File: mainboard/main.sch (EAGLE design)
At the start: 4 parts, among them J1 501645-2620, J2 RJHSE-3380, J3 RJHSE-3380

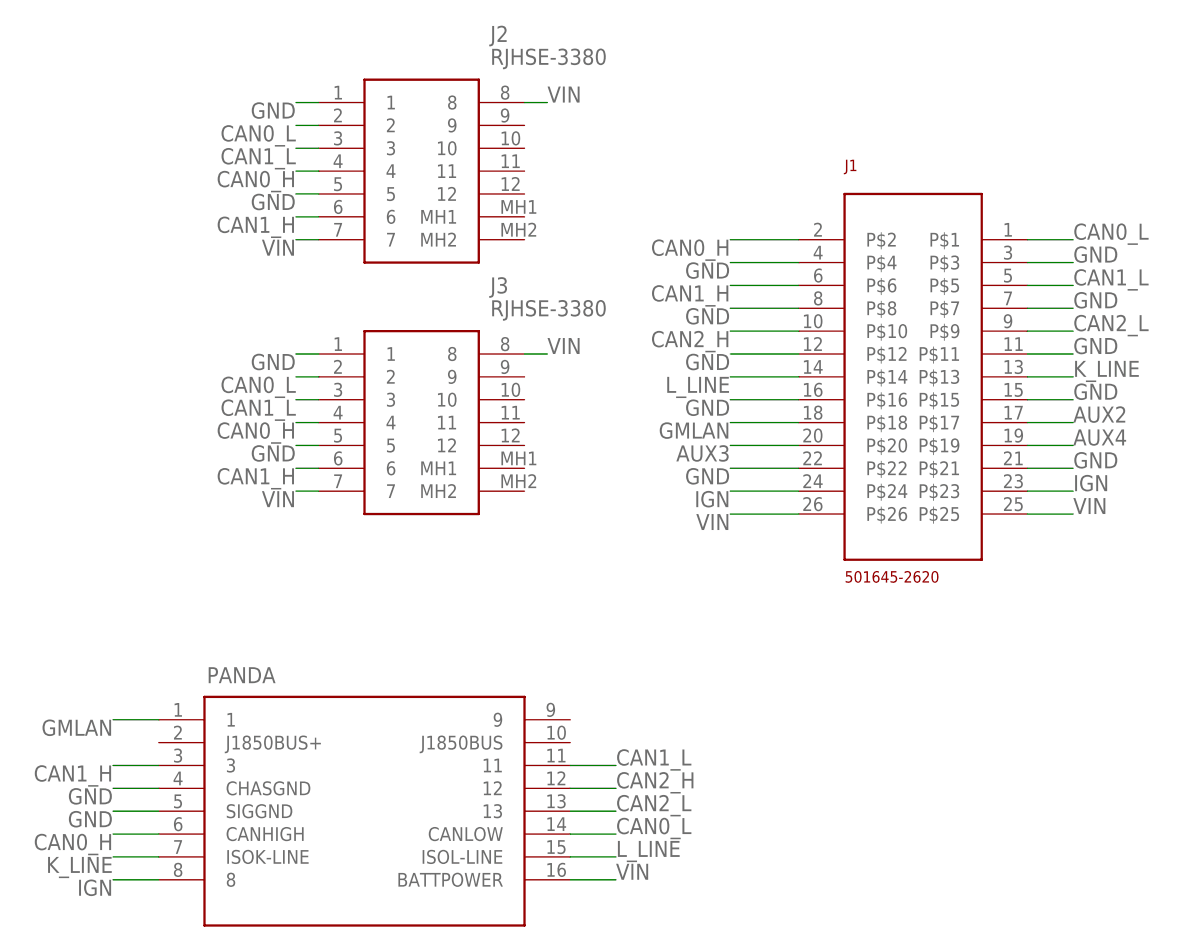
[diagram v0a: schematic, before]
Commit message: switch to rj45 for the interconnect
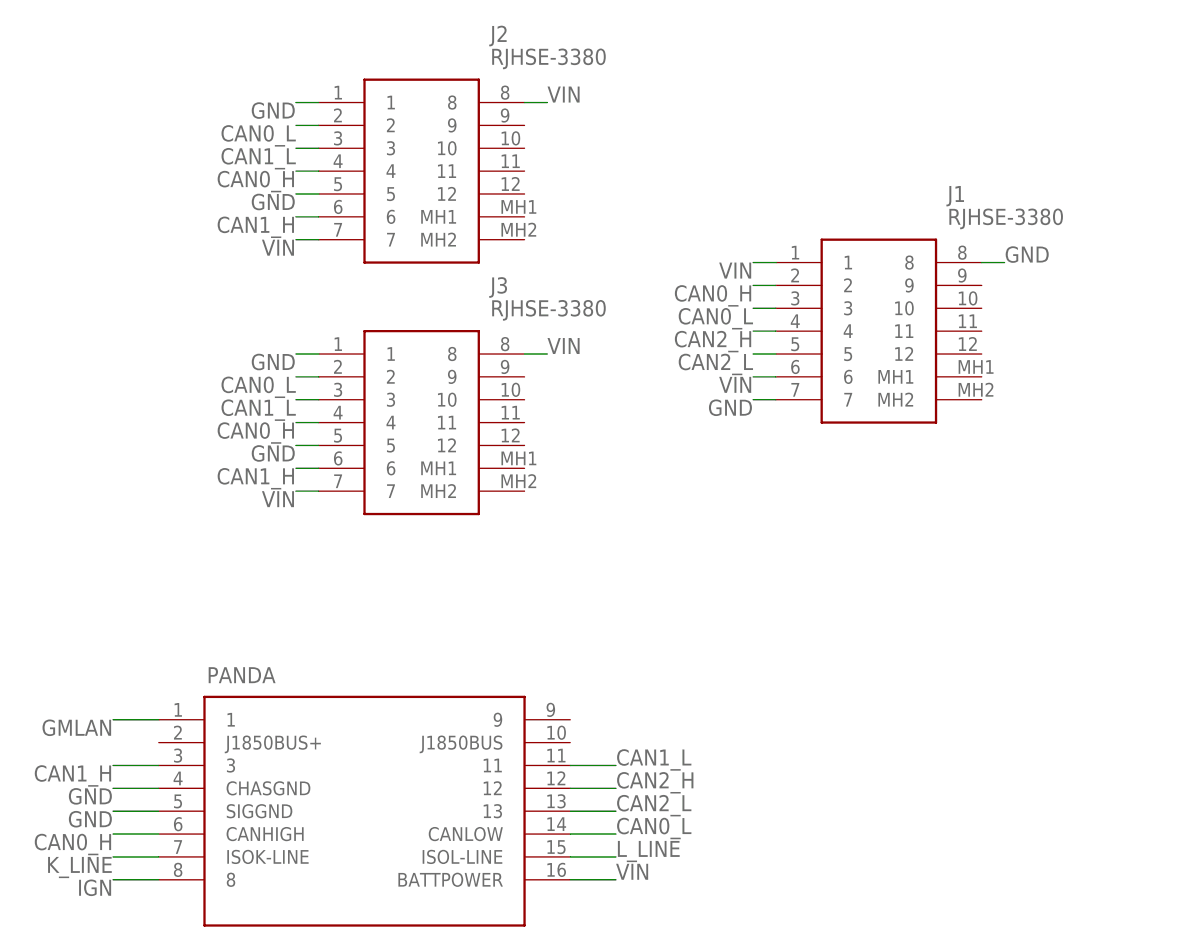
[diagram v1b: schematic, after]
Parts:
- J1: value 501645-2620 -> RJHSE-3380; device Souers:501645-2620 -> RJHSE-3380:RJHSE-3380
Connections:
- removed net AUX2: J1.P$17
- removed net AUX3: J1.P$20
- removed net AUX4: J1.P$19
- net CAN0_H: now also J1.2; no longer J1.P$2
- net CAN0_L: now also J1.3; no longer J1.P$1
- net CAN1_H: no longer J1.P$6
- net CAN1_L: no longer J1.P$5
- net CAN2_H: now also J1.4; no longer J1.P$10
- net CAN2_L: now also J1.5; no longer J1.P$9
- net GMLAN: no longer J1.P$18
- net GND: now also J1.7, J1.8; no longer J1.P$11, J1.P$12, J1.P$15, J1.P$16, J1.P$21, J1.P$22, J1.P$3, J1.P$4, J1.P$7, J1.P$8
- net IGN: no longer J1.P$23, J1.P$24
- net K_LINE: no longer J1.P$13
- net L_LINE: no longer J1.P$14
- net VIN: now also J1.1, J1.6; no longer J1.P$25, J1.P$26
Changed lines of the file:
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@@
 <parts>
 <part name="PANDA" library="comma.ai" deviceset="OBDII-FEMALE" device="FEMALE"/>
-<part name="J1" library="Souers" deviceset="501645-2620" device=""/>
 <part name="J2" library="RJHSE-3380" deviceset="RJHSE-3380" device=""/>
 <part name="J3" library="RJHSE-3380" deviceset="RJHSE-3380" device=""/>
+<part name="J1" library="RJHSE-3380" deviceset="RJHSE-3380" device=""/>
 </parts>
 <sheets>
@@
 <instances>
 <instance part="PANDA" gate="G$1" x="-25.4" y="12.7"/>
-<instance part="J1" gate="G$1" x="30.48" y="58.42"/>
 <instance part="J2" gate="G$1" x="-30.48" y="91.44"/>
 <instance part="J3" gate="G$1" x="-30.48" y="63.5"/>
+<instance part="J1" gate="G$1" x="20.32" y="73.66"/>
 </instances>
 <busses>
@@
 </segment>
 <segment>
-<pinref part="J1" gate="G$1" pin="P$3"/>
-<wire x1="48.26" y1="73.66" x2="53.34" y2="73.66" width="0.1524" layer="91"/>
-<label x="53.34" y="73.66" size="1.778" layer="95"/>
-</segment>
-<segment>
-<pinref part="J1" gate="G$1" pin="P$4"/>
-<wire x1="22.86" y1="73.66" x2="15.24" y2="73.66" width="0.1524" layer="91"/>
-<label x="15.24" y="73.66" size="1.778" layer="95" rot="R180"/>
-</segment>
-<segment>
-<pinref part="J1" gate="G$1" pin="P$8"/>
-<wire x1="22.86" y1="68.58" x2="15.24" y2="68.58" width="0.1524" layer="91"/>
-<label x="15.24" y="68.58" size="1.778" layer="95" rot="R180"/>
-</segment>
-<segment>
-<pinref part="J1" gate="G$1" pin="P$7"/>
-<wire x1="48.26" y1="68.58" x2="53.34" y2="68.58" width="0.1524" layer="91"/>
-<label x="53.34" y="68.58" size="1.778" layer="95"/>
-</segment>
-<segment>
-<pinref part="J1" gate="G$1" pin="P$11"/>
-<wire x1="48.26" y1="63.5" x2="53.34" y2="63.5" width="0.1524" layer="91"/>
-<label x="53.34" y="63.5" size="1.778" layer="95"/>
-</segment>
-<segment>
-<pinref part="J1" gate="G$1" pin="P$12"/>
-<wire x1="22.86" y1="63.5" x2="15.24" y2="63.5" width="0.1524" layer="91"/>
-<label x="15.24" y="63.5" size="1.778" layer="95" rot="R180"/>
-</segment>
-<segment>
-<pinref part="J1" gate="G$1" pin="P$21"/>
-<wire x1="48.26" y1="50.8" x2="53.34" y2="50.8" width="0.1524" layer="91"/>
-<label x="53.34" y="50.8" size="1.778" layer="95"/>
-</segment>
-<segment>
-<pinref part="J1" gate="G$1" pin="P$22"/>
-<wire x1="22.86" y1="50.8" x2="15.24" y2="50.8" width="0.1524" layer="91"/>
-<label x="15.24" y="50.8" size="1.778" layer="95" rot="R180"/>
-</segment>
-<segment>
-<pinref part="J1" gate="G$1" pin="P$16"/>
-<wire x1="22.86" y1="58.42" x2="15.24" y2="58.42" width="0.1524" layer="91"/>
-<label x="15.24" y="58.42" size="1.778" layer="95" rot="R180"/>
-</segment>
-<segment>
-<pinref part="J1" gate="G$1" pin="P$15"/>
-<wire x1="48.26" y1="58.42" x2="53.34" y2="58.42" width="0.1524" layer="91"/>
-<label x="53.34" y="58.42" size="1.778" layer="95"/>
-</segment>
-<segment>
 <pinref part="J2" gate="G$1" pin="1"/>
 <wire x1="-30.48" y1="91.44" x2="-33.02" y2="91.44" width="0.1524" layer="91"/>
@@
 <label x="-33.02" y="53.34" size="1.778" layer="95" rot="R180"/>
 </segment>
+<segment>
+<pinref part="J1" gate="G$1" pin="8"/>
+<wire x1="43.18" y1="73.66" x2="45.72" y2="73.66" width="0.1524" layer="91"/>
+<label x="45.72" y="73.66" size="1.778" layer="95"/>
+</segment>
+<segment>
+<pinref part="J1" gate="G$1" pin="7"/>
+<wire x1="20.32" y1="58.42" x2="17.78" y2="58.42" width="0.1524" layer="91"/>
+<label x="17.78" y="58.42" size="1.778" layer="95" rot="R180"/>
+</segment>
 </net>
 <net name="L_LINE" class="0">
@@
 <label x="2.54" y="7.62" size="1.778" layer="95"/>
 </segment>
-<segment>
-<pinref part="J1" gate="G$1" pin="P$14"/>
-<wire x1="22.86" y1="60.96" x2="15.24" y2="60.96" width="0.1524" layer="91"/>
-<label x="15.24" y="60.96" size="1.778" layer="95" rot="R180"/>
-</segment>
 </net>
 <net name="K_LINE" class="0">
@@
 <label x="-53.34" y="7.62" size="1.778" layer="95" rot="R180"/>
 </segment>
-<segment>
-<pinref part="J1" gate="G$1" pin="P$13"/>
-<wire x1="48.26" y1="60.96" x2="53.34" y2="60.96" width="0.1524" layer="91"/>
-<label x="53.34" y="60.96" size="1.778" layer="95"/>
-</segment>
 </net>
 <net name="IGN" class="1">
@@
 <label x="-53.34" y="5.08" size="1.778" layer="95" rot="R180"/>
 </segment>
-<segment>
-<pinref part="J1" gate="G$1" pin="P$23"/>
-<wire x1="48.26" y1="48.26" x2="53.34" y2="48.26" width="0.1524" layer="91"/>
-<label x="53.34" y="48.26" size="1.778" layer="95"/>
-</segment>
-<segment>
-<pinref part="J1" gate="G$1" pin="P$24"/>
-<wire x1="22.86" y1="48.26" x2="15.24" y2="48.26" width="0.1524" layer="91"/>
-<label x="15.24" y="48.26" size="1.778" layer="95" rot="R180"/>
-</segment>
 </net>
 <net name="VIN" class="1">
@@
 </segment>
 <segment>
-<pinref part="J1" gate="G$1" pin="P$25"/>
-<wire x1="48.26" y1="45.72" x2="53.34" y2="45.72" width="0.1524" layer="91"/>
-<label x="53.34" y="45.72" size="1.778" layer="95"/>
-</segment>
-<segment>
-<pinref part="J1" gate="G$1" pin="P$26"/>
-<wire x1="22.86" y1="45.72" x2="15.24" y2="45.72" width="0.1524" layer="91"/>
-<label x="15.24" y="45.72" size="1.778" layer="95" rot="R180"/>
-</segment>
-<segment>
 <pinref part="J2" gate="G$1" pin="7"/>
 <wire x1="-30.48" y1="76.2" x2="-33.02" y2="76.2" width="0.1524" layer="91"/>
@@
 <label x="-5.08" y="63.5" size="1.778" layer="95"/>
 </segment>
+<segment>
+<pinref part="J1" gate="G$1" pin="1"/>
+<wire x1="20.32" y1="73.66" x2="17.78" y2="73.66" width="0.1524" layer="91"/>
+<label x="17.78" y="73.66" size="1.778" layer="95" rot="R180"/>
+</segment>
+<segment>
+<pinref part="J1" gate="G$1" pin="6"/>
+<wire x1="20.32" y1="60.96" x2="17.78" y2="60.96" width="0.1524" layer="91"/>
+<label x="17.78" y="60.96" size="1.778" layer="95" rot="R180"/>
+</segment>
 </net>
 <net name="CAN2_H" class="0">
@@
 </segment>
 <segment>
-<pinref part="J1" gate="G$1" pin="P$10"/>
-<wire x1="22.86" y1="66.04" x2="15.24" y2="66.04" width="0.1524" layer="91"/>
-<label x="15.24" y="66.04" size="1.778" layer="95" rot="R180"/>
+<pinref part="J1" gate="G$1" pin="4"/>
+<wire x1="20.32" y1="66.04" x2="17.78" y2="66.04" width="0.1524" layer="91"/>
+<label x="17.78" y="66.04" size="1.778" layer="95" rot="R180"/>
 </segment>
 </net>
@@
 </segment>
 <segment>
-<pinref part="J1" gate="G$1" pin="P$9"/>
-<wire x1="48.26" y1="66.04" x2="53.34" y2="66.04" width="0.1524" layer="91"/>
-<label x="53.34" y="66.04" size="1.778" layer="95"/>
+<pinref part="J1" gate="G$1" pin="5"/>
+<wire x1="20.32" y1="63.5" x2="17.78" y2="63.5" width="0.1524" layer="91"/>
+<label x="17.78" y="63.5" size="1.778" layer="95" rot="R180"/>
 </segment>
 </net>
@@
 </segment>
 <segment>
-<pinref part="J1" gate="G$1" pin="P$2"/>
-<wire x1="22.86" y1="76.2" x2="15.24" y2="76.2" width="0.1524" layer="91"/>
-<label x="15.24" y="76.2" size="1.778" layer="95" rot="R180"/>
-</segment>
-<segment>
 <pinref part="J2" gate="G$1" pin="4"/>
 <wire x1="-30.48" y1="83.82" x2="-33.02" y2="83.82" width="0.1524" layer="91"/>
@@
 <label x="-33.02" y="55.88" size="1.778" layer="95" rot="R180"/>
 </segment>
+<segment>
+<pinref part="J1" gate="G$1" pin="2"/>
+<wire x1="20.32" y1="71.12" x2="17.78" y2="71.12" width="0.1524" layer="91"/>
+<label x="17.78" y="71.12" size="1.778" layer="95" rot="R180"/>
+</segment>
 </net>
 <net name="CAN0_L" class="0">
@@
 </segment>
 <segment>
-<pinref part="J1" gate="G$1" pin="P$1"/>
-<wire x1="48.26" y1="76.2" x2="53.34" y2="76.2" width="0.1524" layer="91"/>
-<label x="53.34" y="76.2" size="1.778" layer="95"/>
-</segment>
-<segment>
 <pinref part="J2" gate="G$1" pin="2"/>
 <wire x1="-30.48" y1="88.9" x2="-33.02" y2="88.9" width="0.1524" layer="91"/>
@@
 <label x="-33.02" y="60.96" size="1.778" layer="95" rot="R180"/>
 </segment>
+<segment>
+<pinref part="J1" gate="G$1" pin="3"/>
+<wire x1="20.32" y1="68.58" x2="17.78" y2="68.58" width="0.1524" layer="91"/>
+<label x="17.78" y="68.58" size="1.778" layer="95" rot="R180"/>
+</segment>
 </net>
 <net name="CAN1_L" class="0">
@@
 </segment>
 <segment>
-<pinref part="J1" gate="G$1" pin="P$5"/>
-<wire x1="48.26" y1="71.12" x2="53.34" y2="71.12" width="0.1524" layer="91"/>
-<label x="53.34" y="71.12" size="1.778" layer="95"/>
-</segment>
-<segment>
 <pinref part="J2" gate="G$1" pin="3"/>
 <wire x1="-30.48" y1="86.36" x2="-33.02" y2="86.36" width="0.1524" layer="91"/>
@@
 </segment>
 <segment>
-<pinref part="J1" gate="G$1" pin="P$6"/>
-<wire x1="22.86" y1="71.12" x2="15.24" y2="71.12" width="0.1524" layer="91"/>
-<label x="15.24" y="71.12" size="1.778" layer="95" rot="R180"/>
-</segment>
-<segment>
 <pinref part="J2" gate="G$1" pin="6"/>
 <wire x1="-30.48" y1="78.74" x2="-33.02" y2="78.74" width="0.1524" layer="91"/>
@@
 </segment>
 </net>
-<net name="AUX2" class="0">
-<segment>
-<pinref part="J1" gate="G$1" pin="P$17"/>
-<wire x1="48.26" y1="55.88" x2="53.34" y2="55.88" width="0.1524" layer="91"/>
-<label x="53.34" y="55.88" size="1.778" layer="95"/>
-</segment>
-</net>
-<net name="AUX3" class="0">
-<segment>
-<pinref part="J1" gate="G$1" pin="P$20"/>
-<wire x1="22.86" y1="53.34" x2="15.24" y2="53.34" width="0.1524" layer="91"/>
-<label x="15.24" y="53.34" size="1.778" layer="95" rot="R180"/>
-</segment>
-</net>
-<net name="AUX4" class="0">
-<segment>
-<pinref part="J1" gate="G$1" pin="P$19"/>
-<wire x1="48.26" y1="53.34" x2="53.34" y2="53.34" width="0.1524" layer="91"/>
-<label x="53.34" y="53.34" size="1.778" layer="95"/>
-</segment>
-</net>
 <net name="GMLAN" class="0">
 <segment>
@@
 <label x="-53.34" y="22.86" size="1.778" layer="95" rot="R180"/>
 </segment>
-<segment>
-<pinref part="J1" gate="G$1" pin="P$18"/>
-<wire x1="22.86" y1="55.88" x2="15.24" y2="55.88" width="0.1524" layer="91"/>
-<label x="15.24" y="55.88" size="1.778" layer="95" rot="R180"/>
-</segment>
-</net>
+</net>
